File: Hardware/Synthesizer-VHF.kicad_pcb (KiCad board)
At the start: 2 copper layers, 38.9 x 37.7 mm, 87 parts, among them J1 Screw_Terminal_01x02, J2 Scope, J3 REF Select, J4 USB-C 2.0 16P, J5 REF_IN, J6 Scope, J7 RFOUTA, J8 Header 1x3, J9 RFOUTB, U1 LM7805A, U2 FT231XQ, U3 ATtiny1616-M, U4 ADF4350, U5 GM1200ACPZ, U6 GM1200ACPZ, X1 IQXO-70

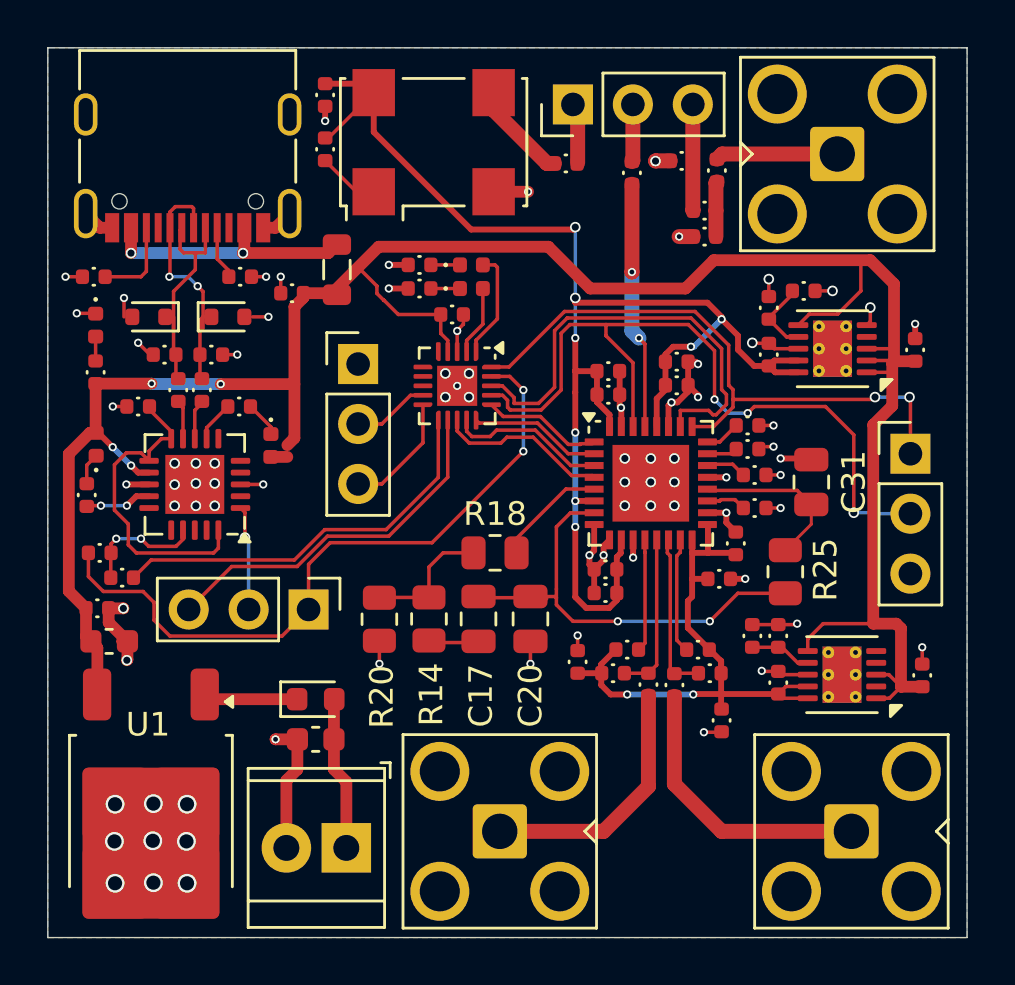
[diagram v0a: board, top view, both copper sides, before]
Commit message: Final version for costing and possible ordering Change TCXO to on available from LCSC
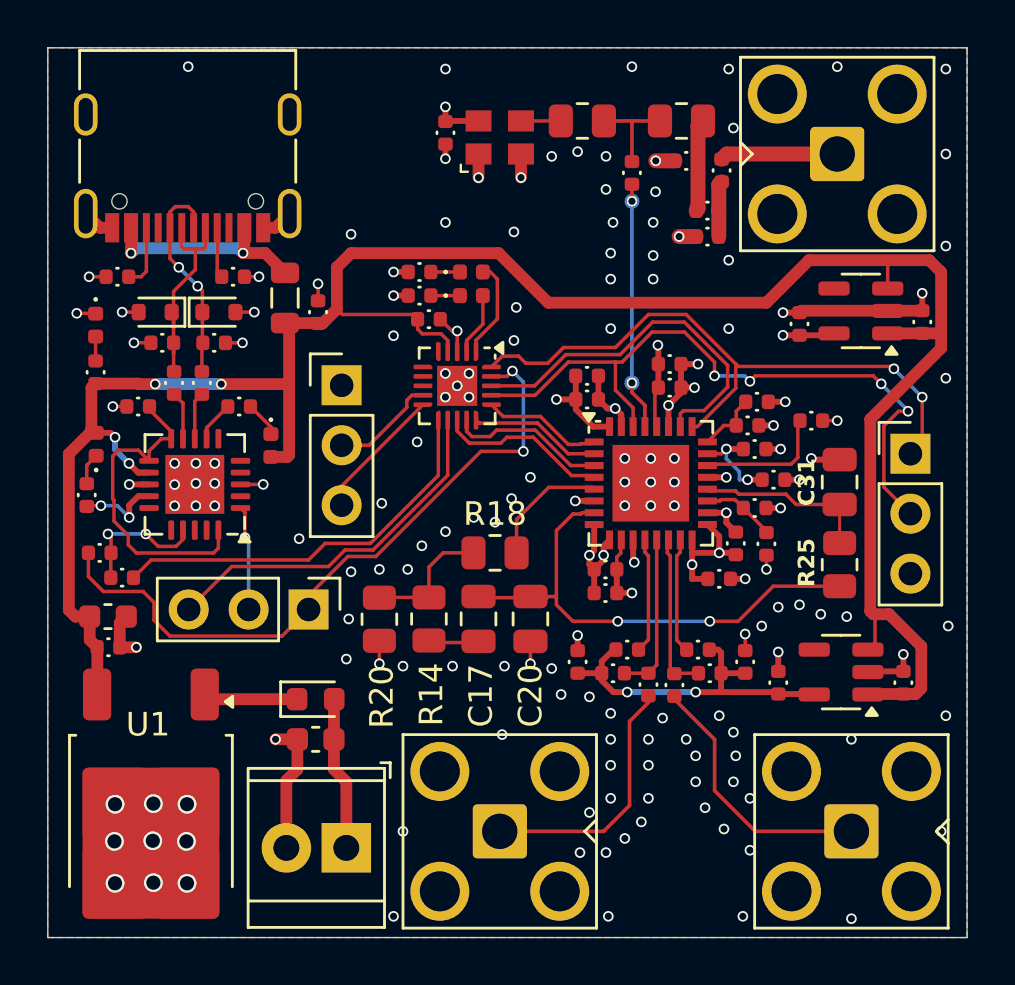
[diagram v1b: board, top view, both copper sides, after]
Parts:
- removed C34, C35: 4.7u 10V, Synthesizer:Cap_0402
- removed J3: REF Select, Connector_PinHeader_2.54mm:PinHeader_1x03_P2.54mm_Vertical
- removed R27: 33K2, Synthesizer:Res_0402
- removed R4: 10K, Synthesizer:Res_0402
- removed U5, U6: GM1200ACPZ, Package_DFN_QFN:DFN-10-1EP_3x3mm_P0.5mm_EP1.65x2.38mm_ThermalVias
- added C36: 100n, Synthesizer:Cap_0402, F.Cu at (164.6, 91.0)
- added C37: 10p, Synthesizer:Cap_0402, F.Cu at (165.0, 97.0)
- added C38: 100n, Synthesizer:Cap_0402, F.Cu at (165.3, 94.3)
- added U7: ADP150AUJZ-3.3-R7, Package_TO_SOT_SMD:SOT-23-5, F.Cu at (169.0, 87.2)
- added U8: ADP150AUJZ-3.3-R7, Package_TO_SOT_SMD:SOT-23-5, F.Cu at (168.2, 102.5)
- C10, C26: value 100n -> 10p
- C13, C18, C25, C30: value 10n -> 100n
- C14, C27, C32, C33: value 4.7u 10V -> 1u 10V
- C19, C21, C24, C28: value 100p -> 10p
- R11, R15, R21, R23, R5: value 51R -> 49R9
- R2: footprint Synthesizer:Res_0402 -> Resistor_SMD:R_0805_2012Metric
- R22: value 5k1 -> 4K7
- R26: value 33K2 -> NP; footprint Synthesizer:Res_0402 -> Resistor_SMD:R_0805_2012Metric
- X1: value IQXO-70 -> HCI 8122S-25NQ33FTL; footprint Synthesizer:Oscillator_SMD_IQD_IQXO70-4Pin_7.5x5.0mm -> Synthesizer:Oscillator_SMD2520
- moved R26 22.0 mm to (161.4, 79.1), turned to 0 degrees
- moved C5 5.34 mm to (151.4, 79.6)
- moved R22 3.32 mm to (166.9, 91.8)
- moved X1 2.81 mm to (153.7, 79.8)
- moved C22 2.67 mm to (164.1, 102.0), turned to 90 degrees
- moved FB1 2.51 mm to (144.6, 86.6)
- moved R25 2.32 mm to (168.1, 97.9)
- moved R2 1.93 mm to (157.2, 79.1)
- moved C27 1.84 mm to (166.4, 87.7)
- moved C6 1.71 mm to (137.1, 101.4)
- moved C2 1.36 mm to (146.0, 87.2), turned to 90 degrees
- moved C32 1.22 mm to (171.6, 87.6)
- moved C31 1.20 mm to (168.1, 94.4)
- moved J6 1.14 mm to (147.0, 90.3)
- moved C8 1.05 mm to (137.1, 100.1)
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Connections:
- C13 pad 1: /VCC_DIG -> /VCC_1
- C14 pad 1: /VCC_RF -> /VCC_2
- C15 pad 1: /VCC_RF -> /VCC_2
- C18 pad 1: /VCC_RF -> /VCC_1
- C19 pad 2: /VCC_DIG -> /VCC_1
- C21 pad 2: /VCC_DIG -> /VCC_1
- C22 pad 1: /VCC_RF -> /VCC_2
- C24 pad 1: /VCC_DIG -> /VCC_1
- C25 pad 1: /VCC_DIG -> /VCC_1
- C27 pad 1: /VCC_DIG -> /VCC_1
- C28 pad 2: /VCC_RF -> /VCC_1
- C3 pad 2: Net-(J3-Pin_2) -> Net-(C3-Pad2)
- C30 pad 1: /VCC_DIG -> /VCC_1
- C5 pad 2: /VCC_DIG -> /VCC_1
- R11 pad 2: /VCC_RF -> /VCC_2
- R15 pad 2: /VCC_RF -> /VCC_2
- R2 pad 2: Net-(J3-Pin_1) -> Net-(C3-Pad2)
- R21 pad 2: /VCC_RF -> /VCC_2
- R23 pad 2: /VCC_RF -> /VCC_2
- R26 pad 1: GND -> Net-(C3-Pad2)
- R26 pad 2: Net-(U6-SET) -> Net-(R26-Pad2)
- R6 pad 1: Net-(J3-Pin_3) -> Net-(R26-Pad2)
- R7 pad 2: Net-(J3-Pin_3) -> Net-(R26-Pad2)
- U4 pad 10: /VCC_DIG -> /VCC_1
- U4 pad 16: /VCC_RF -> /VCC_1
- U4 pad 17: /VCC_RF -> /VCC_1
- U4 pad 28: /VCC_DIG -> /VCC_1
- U4 pad 32: /VCC_DIG -> /VCC_1
- U4 pad 6: /VCC_DIG -> /VCC_1
- X1 pad 1: Net-(X1-E/B) -> GND
- X1 pad 4: /VCC_DIG -> /VCC_1
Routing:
- net /VCC_DIG: track 61.3 -> 0.00 mm, vias 8 -> 0
- net /VCC_RF: track 25.3 -> 0.00 mm, vias 2 -> 0
- net /VCC_1: track 0.00 -> 20.8 mm, vias 0 -> 8
- net /VCC_2: track 0.00 -> 15.1 mm, vias 0 -> 2
- net Net-(J3-Pin_3): track 4.51 -> 0.00 mm
- net Net-(C3-Pad2): track 0.00 -> 4.10 mm
- net Net-(R26-Pad2): track 0.00 -> 3.92 mm
- net Net-(U4-RSET): track 1.73 -> 5.57 mm
- net /MUX: track 32.6 -> 29.3 mm, vias 3 -> 4
- net Net-(U5-SET): track 3.17 -> 0.00 mm
- net /RF_EN: track 19.0 -> 15.8 mm
- net Net-(U4-VCOM): track 1.30 -> 4.10 mm, vias 0 -> 2
- net /5V: track 100.9 -> 98.3 mm
- net Net-(U6-SET): track 2.62 -> 0.00 mm
- net Net-(X1-E/B): track 2.60 -> 0.00 mm
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- added copper zone on In2.Cu, net /VCC_1
- added copper zone on F.Cu, net GND
- added copper zone on In1.Cu, net GND
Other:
- copper layers 2 -> 4

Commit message: This what got sent to fab.  The wiring for SPI between MCU and ADF4351 is not connected to the hardware SPI pins and will need bit banging.
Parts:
- D3: value White -> blue
- U4: value ADF4350 -> ADF4351
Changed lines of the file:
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@@
 			)
 		)
-		(property "LCSC" "C15195"
+		(property "LCSC" "C1525"
 			(at 0 0 0)
 			(layer "F.SilkS")
@@
 			)
 		)
-		(property "LCSC" "C14663"
+		(property "LCSC" "C1525"
 			(at 0 0 0)
 			(unlocked yes)
@@
 			)
 		)
-		(property "LCSC" "C2290"
+		(property "LCSC" "C364550"
 			(at 0 0 0)
 			(unlocked yes)
@@
 			)
 		)
-		(property "LCSC" "C21190"
+		(property "LCSC" "C11702"
 			(at 0 0 0)
 			(unlocked yes)
@@
 			)
 		)
-		(property "LCSC" "C21190"
+		(property "LCSC" "C11702"
 			(at 0 0 180)
 			(unlocked yes)
@@
 			)
 		)
-		(property "LCSC" "C15195"
-			(at 0 0 360)
+		(property "LCSC" "C1525"
+			(at 0 0 0)
 			(layer "F.SilkS")
 			(hide yes)
@@
 			)
 		)
-		(property "LCSC" "C2290"
+		(property "LCSC" "C364550"
 			(at 0 0 0)
 			(unlocked yes)
@@
 			)
 		)
-		(property "LCSC" "C32949"
+		(property "LCSC" "C1546"
 			(at 0 0 0)
 			(layer "F.SilkS")
@@
 			)
 		)
-		(property "LCSC" ""
+		(property "LCSC" "C282682"
 			(at 0 0 180)
 			(unlocked yes)
@@
 		(sheetname "Root")
 		(sheetfile "Synthesizer-VHF.kicad_sch")
-		(attr smd exclude_from_pos_files)
+		(attr smd exclude_from_pos_files exclude_from_bom dnp)
 		(fp_line
 			(start -0.227064 -0.735)
@@
 			)
 		)
-		(property "LCSC" "C1671"
+		(property "LCSC" "C1567"
 			(at 0 0 180)
 			(unlocked yes)
@@
 			)
 		)
-		(property "Value" "White"
+		(property "Value" "blue"
 			(at 0 1.17 90)
 			(layer "F.Fab")
@@
 			)
 		)
-		(property "LCSC" "C2290"
+		(property "LCSC" "C364550"
 			(at 0 0 -90)
 			(unlocked yes)
@@
 			)
 		)
-		(property "LCSC" "C21190"
+		(property "LCSC" "C11702"
 			(at 0 0 0)
 			(unlocked yes)
@@
 			)
 		)
-		(property "LCSC" "C23186"
+		(property "LCSC" "C105872"
 			(at 0 0 180)
 			(unlocked yes)
@@
 			)
 		)
-		(property "LCSC" "C23345"
+		(property "LCSC" "C93929"
 			(at 0 0 90)
 			(unlocked yes)
@@
 			)
 		)
-		(property "Value" "ADF4350"
+		(property "Value" "ADF4351"
 			(at 0 3.75 0)
 			(layer "F.Fab")
@@
 			)
 		)
-		(property "Datasheet" "https://www.analog.com/media/en/technical-documentation/data-sheets/ADF4350.pdf"
+		(property "Datasheet" "https://www.analog.com/media/en/technical-documentation/data-sheets/ADF4351.pdf"
 			(at 0 0 0)
 			(unlocked yes)
@@
 			)
 		)
-		(property "Description" "137.5-4400MHz fractional-N PLL, LFCSP-32"
+		(property "Description" "Wideband Synthesizerwith Integrated VCO"
 			(at 0 0 0)
 			(unlocked yes)
@@
 			)
 		)
-		(property "LCSC" "C98705"
+		(property "LCSC" "C654681"
 			(at 0 0 0)
 			(unlocked yes)
@@
 			)
 		)
-		(property "LCSC" "C1525"
+		(property "LCSC" "C32949"
 			(at 0 0 90)
 			(unlocked yes)
@@
 			)
 		)
-		(property "LCSC" "C15195"
+		(property "LCSC" "C1525"
 			(at 0 0 0)
 			(layer "F.SilkS")
@@
 			)
 		)
-		(property "LCSC" "C17477"
+		(property "LCSC" "C17168"
 			(at 0 0 0)
 			(layer "F.SilkS")
@@
 			)
 		)
-		(property "LCSC" ""
+		(property "LCSC" "C105871"
 			(at 0 0 0)
 			(layer "F.SilkS")
@@
 			)
 		)
-		(property "LCSC" "C14663"
+		(property "LCSC" "C1525"
 			(at 0 0 0)
 			(unlocked yes)
@@
 			)
 		)
-		(property "LCSC" "C21190"
+		(property "LCSC" "C11702"
 			(at 0 0 -90)
 			(unlocked yes)
@@
 			)
 		)
-		(property "LCSC" "C72038"
+		(property "LCSC" "C434449"
 			(at 0 0 90)
 			(unlocked yes)
@@
 			)
 		)
-		(property "LCSC" ""
+		(property "LCSC" "C52923"
 			(at 0 0 0)
 			(layer "F.SilkS")
@@
 			)
 		)
-		(property "LCSC" "C12530"
+		(property "LCSC" "C52923"
 			(at 0 0 0)
 			(layer "F.SilkS")
@@
 			)
 		)
-		(property "LCSC" "C1525"
+		(property "LCSC" "C32949"
 			(at 0 0 0)
 			(layer "F.SilkS")
@@
 			)
 		)
-		(property "LCSC" "C15195"
+		(property "LCSC" "C1525"
 			(at 0 0 0)
 			(unlocked yes)
@@
 			)
 		)
-		(property "LCSC" "C14663"
+		(property "LCSC" "C1525"
 			(at 0 0 180)
 			(unlocked yes)
@@
 		(tags "SOT TO_SOT_SMD")
 		(property "Reference" "U8"
-			(at 0 -2.4 360)
+			(at 0 -2.4 0)
 			(layer "F.SilkS")
 			(hide yes)
@@
 		)
 		(property "Value" "ADP150AUJZ-3.3-R7"
-			(at 0 2.4 360)
+			(at 0 2.4 0)
 			(layer "F.Fab")
 			(hide yes)
@@
 		)
 		(property "Footprint" "Package_TO_SOT_SMD:SOT-23-5"
-			(at 0 0 360)
+			(at 0 0 0)
 			(layer "F.Fab")
 			(hide yes)
@@
 		)
 		(property "Datasheet" "https://www.analog.com/media/en/technical-documentation/data-sheets/adp150.pdf"
-			(at 0 0 360)
+			(at 0 0 0)
 			(layer "F.Fab")
 			(hide yes)
@@
 		)
 		(property "Description" "150mA Fixed 3.3V, 5.5V in, TSOT-23-5 Regulator"
-			(at 0 0 360)
+			(at 0 0 0)
 			(layer "F.Fab")
 			(hide yes)
@@
 		)
 		(fp_text user "${REFERENCE}"
-			(at 0 0 360)
+			(at 0 0 0)
 			(layer "F.Fab")
 			(effects
@@
 			)
 		)
-		(property "LCSC" "C15195"
+		(property "LCSC" "C1525"
 			(at 0 0 0)
 			(layer "F.SilkS")
@@
 			)
 		)
-		(property "LCSC" "C15195"
+		(property "LCSC" "C32949"
 			(at 0 0 0)
 			(layer "F.SilkS")
@@
 			)
 		)
-		(property "LCSC" "C1671"
+		(property "LCSC" "C1567"
 			(at 0 0 0)
 			(unlocked yes)
@@
 			)
 		)
-		(property "LCSC" "C116949"
+		(property "LCSC" "C22395574"
 			(at 0 0 180)
 			(unlocked yes)
@@
 			)
 		)
-		(property "LCSC" "C21190"
+		(property "LCSC" "C11702"
 			(at 0 0 180)
 			(unlocked yes)
@@
 			)
 		)
-		(property "LCSC" "C15195"
+		(property "LCSC" "C1525"
 			(at 0 0 0)
 			(layer "F.SilkS")
@@
 		(sheetname "Root")
 		(sheetfile "Synthesizer-VHF.kicad_sch")
-		(attr smd exclude_from_pos_files)
+		(attr smd)
 		(fp_line
 			(start -0.227064 -0.735)
@@
 			)
 		)
-		(property "LCSC" "C14663"
+		(property "LCSC" "C1525"
 			(at 0 0 90)
 			(unlocked yes)
@@
 			)
 		)
-		(property "LCSC" "C23186"
+		(property "LCSC" "C105872"
 			(at 0 0 0)
 			(unlocked yes)
@@
 		(tags "SOT TO_SOT_SMD")
 		(property "Reference" "U7"
-			(at 0 -2.4 360)
+			(at 0 -2.4 0)
 			(layer "F.SilkS")
 			(hide yes)
@@
 		)
 		(property "Value" "ADP150AUJZ-3.3-R7"
-			(at 0 2.4 360)
+			(at 0 2.4 0)
 			(layer "F.Fab")
 			(hide yes)
@@
 		)
 		(property "Footprint" "Package_TO_SOT_SMD:SOT-23-5"
-			(at 0 0 360)
+			(at 0 0 0)
 			(layer "F.Fab")
 			(hide yes)
@@
 		)
 		(property "Datasheet" "https://www.analog.com/media/en/technical-documentation/data-sheets/adp150.pdf"
-			(at 0 0 360)
+			(at 0 0 0)
 			(layer "F.Fab")
 			(hide yes)
@@
 		)
 		(property "Description" "150mA Fixed 3.3V, 5.5V in, TSOT-23-5 Regulator"
-			(at 0 0 360)
+			(at 0 0 0)
 			(layer "F.Fab")
 			(hide yes)
@@
 		)
 		(fp_text user "${REFERENCE}"
-			(at 0 0 360)
+			(at 0 0 0)
 			(layer "F.Fab")
 			(effects
@@
 			)
 		)
-		(property "LCSC" "C12530"
+		(property "LCSC" "C52923"
 			(at 0 0 0)
 			(layer "F.SilkS")
@@
 			)
 		)
-		(property "LCSC" "C32949"
+		(property "LCSC" "C1546"
 			(at 0 0 0)
 			(layer "F.SilkS")
@@
 			)
 		)
-		(property "LCSC" "C12530"
+		(property "LCSC" "C52923"
 			(at 0 0 0)
 			(layer "F.SilkS")
@@
 			)
 		)
-		(property "LCSC" "C21190"
+		(property "LCSC" "C11702"
 			(at 0 0 90)
 			(unlocked yes)
@@
 			)
 		)
-		(property "LCSC" "C21190"
+		(property "LCSC" "C11702"
 			(at 0 0 180)
 			(unlocked yes)
@@
 		(sheetname "Root")
 		(sheetfile "Synthesizer-VHF.kicad_sch")
-		(attr smd)
+		(attr smd exclude_from_pos_files exclude_from_bom dnp)
 		(fp_line
 			(start -0.227064 -0.735)
@@
 			)
 		)
-		(property "LCSC" "C23345"
+		(property "LCSC" "C93929"
 			(at 0 0 90)
 			(unlocked yes)
@@
 			)
 		)
-		(property "LCSC" "C116949"
+		(property "LCSC" "C22395574"
 			(at 0 0 0)
 			(unlocked yes)
@@
 			)
 		)
-		(property "LCSC" "C72038"
+		(property "LCSC" "C434449"
 			(at 0 0 -90)
 			(unlocked yes)
